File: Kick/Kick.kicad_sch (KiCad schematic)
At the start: 11 parts, among them J1 CN1 / J11, J2 CN2 / J12, U0 NOIP1SN1300A-QTI, U1 NOIP1SN1300A-QTI, U2 NX3L4053, U3 NX3L4053, U4 MIC5504-1.8YM5

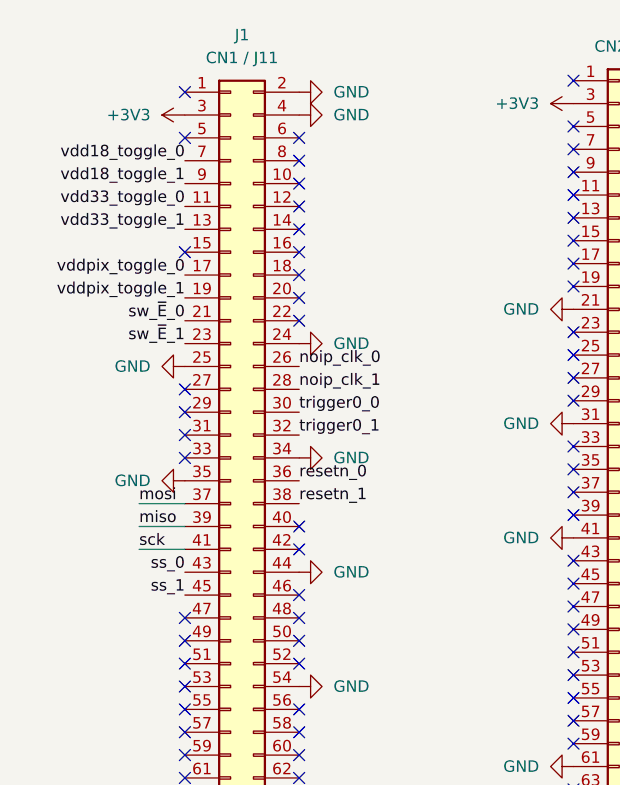
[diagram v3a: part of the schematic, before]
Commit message: routed U1's side and power supply.
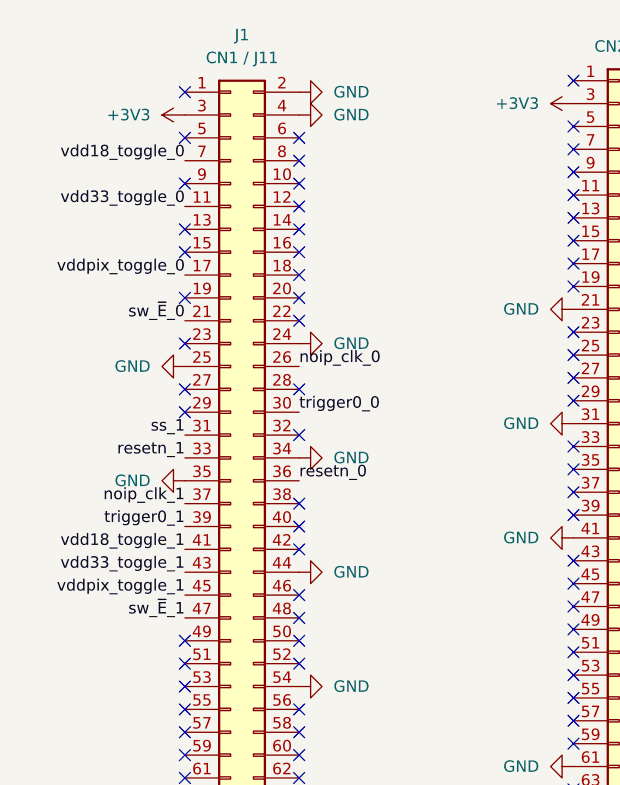
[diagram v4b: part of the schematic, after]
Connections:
- net miso: no longer J1.39 (Pin_39)
- net mosi: no longer J1.37 (Pin_37)
- net noip_clk_1: now also J1.37 (Pin_37); no longer J1.28 (Pin_28)
- net resetn_1: now also J1.33 (Pin_33); no longer J1.38 (Pin_38)
- net sck: no longer J1.41 (Pin_41)
- net ss_0: no longer J1.43 (Pin_43)
- net ss_1: now also J1.31 (Pin_31); no longer J1.45 (Pin_45)
- net sw_~{E}_1: now also J1.47 (Pin_47); no longer J1.23 (Pin_23)
- net trigger0_1: now also J1.39 (Pin_39); no longer J1.32 (Pin_32)
- net vdd18_toggle_1: now also J1.41 (Pin_41); no longer J1.9 (Pin_9)
- net vdd33_toggle_1: now also J1.43 (Pin_43); no longer J1.13 (Pin_13)
- net vddpix_toggle_1: now also J1.45 (Pin_45); no longer J1.19 (Pin_19)
- no-connect marks 102 -> 106

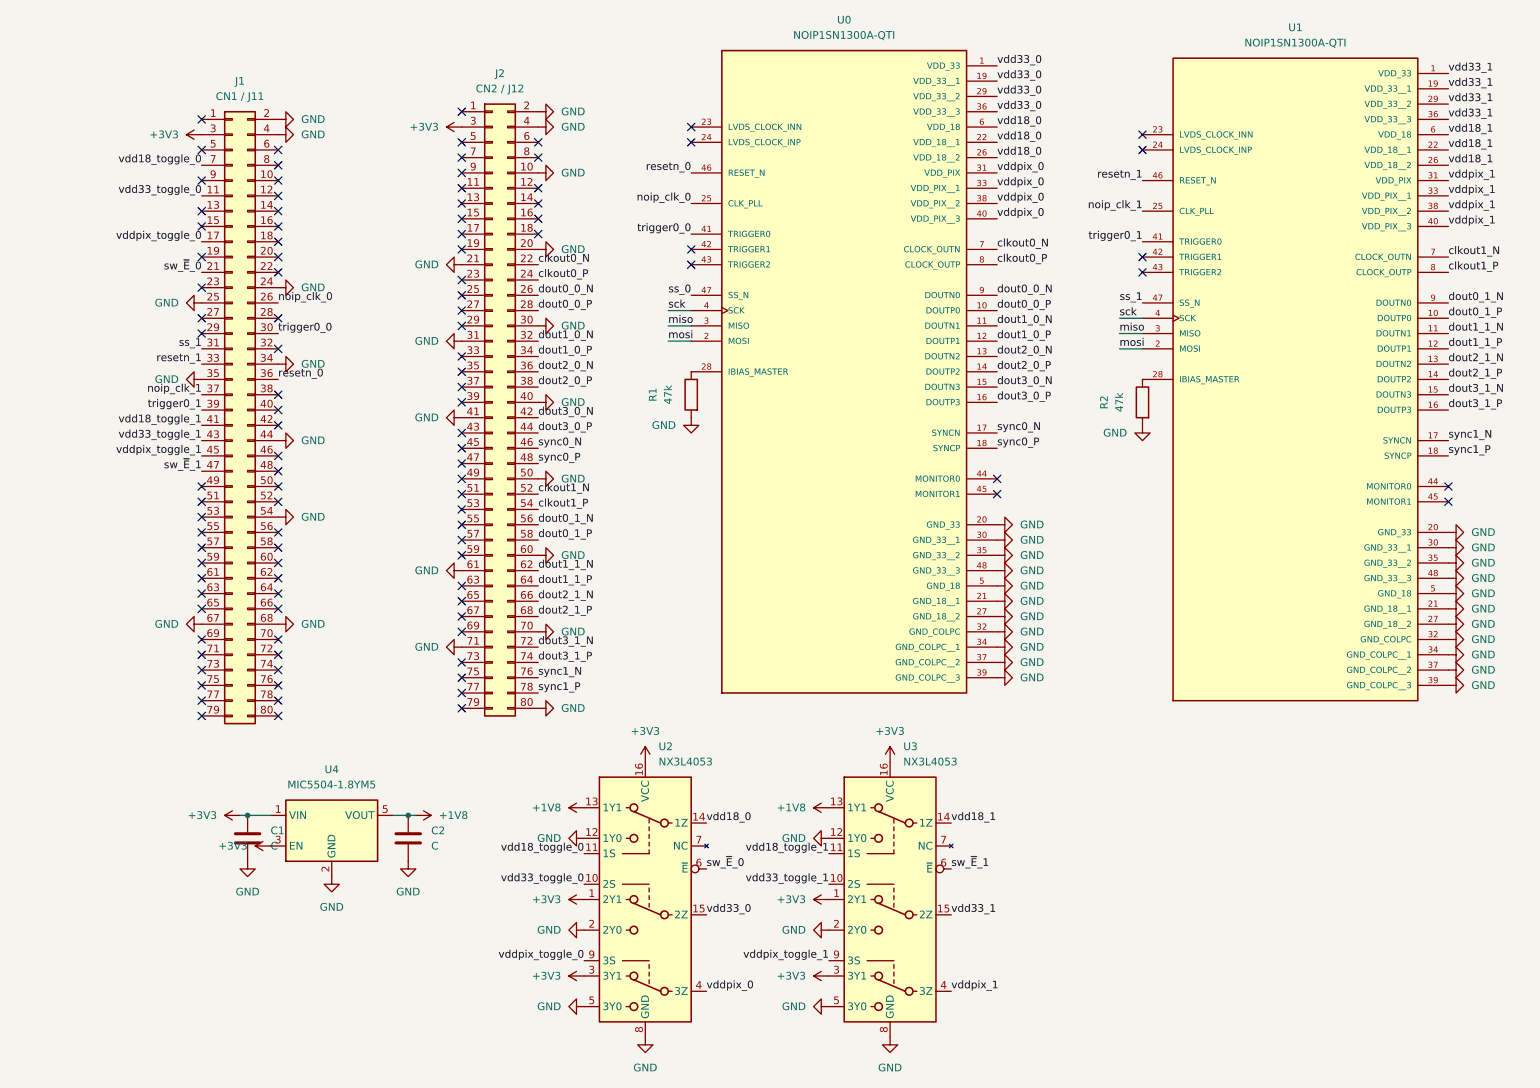
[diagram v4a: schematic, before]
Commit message: preliminary routing (lacking spi and monitors), prior to setting correct distance between sensors
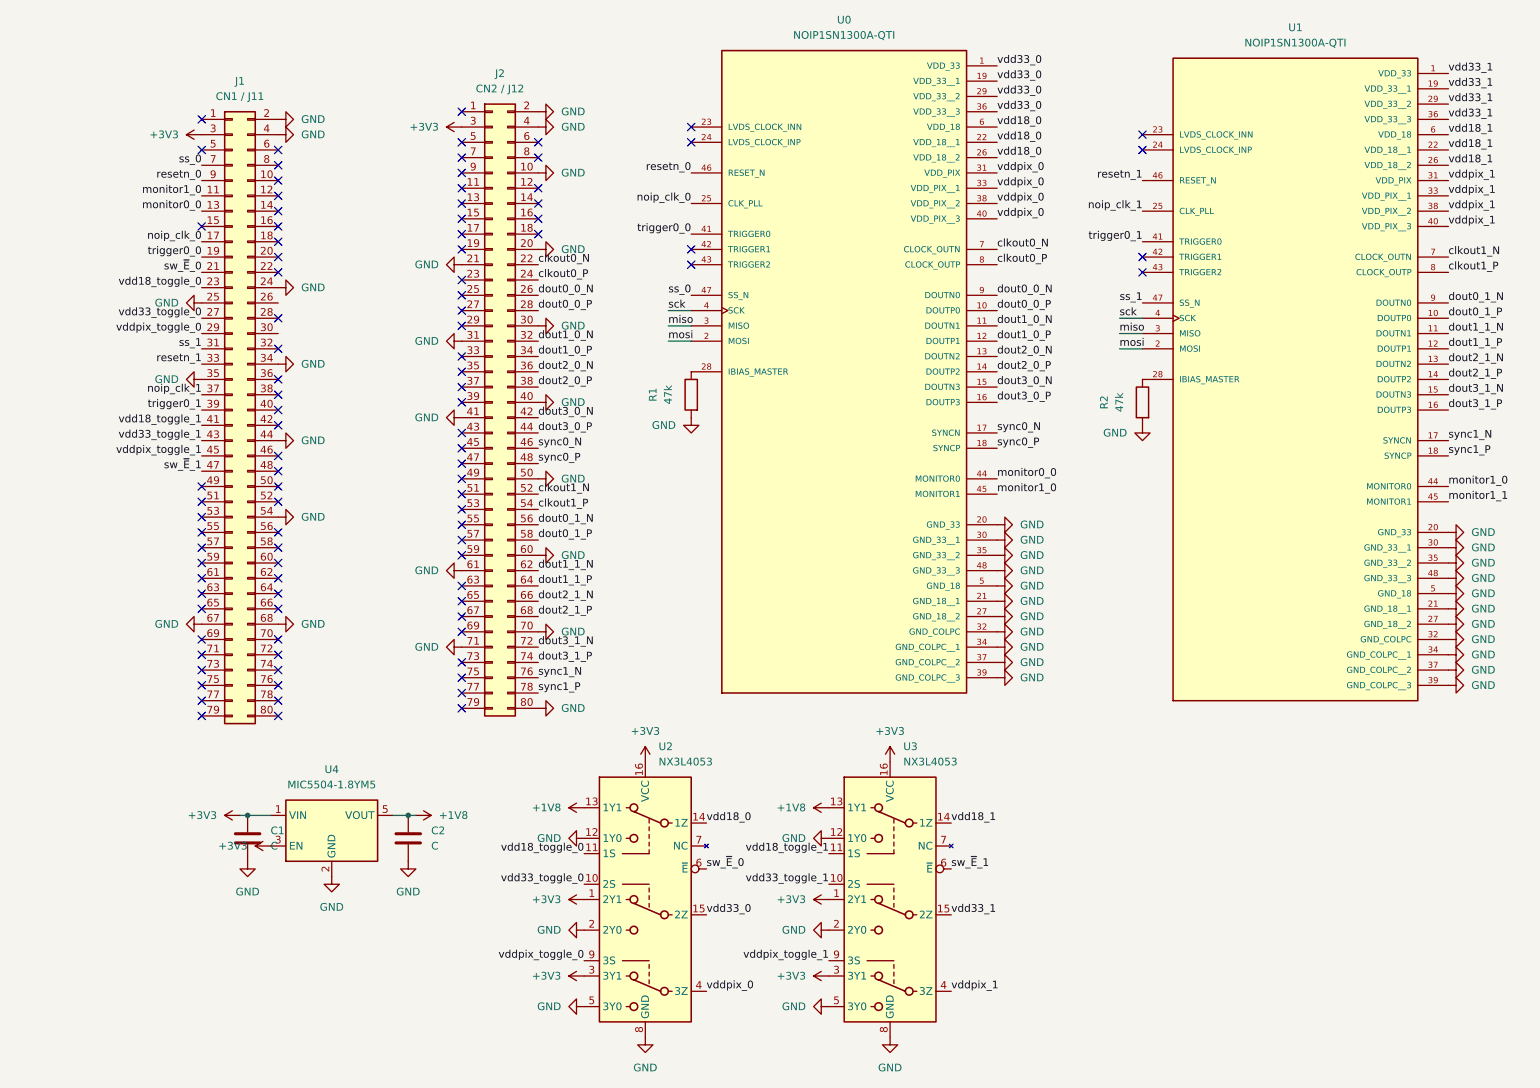
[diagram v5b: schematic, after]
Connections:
- net noip_clk_0: now also J1.17 (Pin_17); no longer J1.26 (Pin_26)
- net resetn_0: now also J1.9 (Pin_9); no longer J1.36 (Pin_36)
- net ss_0: now also J1.7 (Pin_7)
- net trigger0_0: now also J1.19 (Pin_19); no longer J1.30 (Pin_30)
- net vdd18_toggle_0: now also J1.23 (Pin_23); no longer J1.7 (Pin_7)
- net vdd33_toggle_0: now also J1.27 (Pin_27); no longer J1.11 (Pin_11)
- net vddpix_toggle_0: now also J1.29 (Pin_29); no longer J1.17 (Pin_17)
- net monitor0_0: now reaches J1.13 (Pin_13)
- net monitor0_0: now also U0.44 (MONITOR0)
- net monitor1_0: now reaches U0.45 (MONITOR1)
- net monitor1_0: now also J1.11 (Pin_11), U1.44 (MONITOR0)
- net monitor1_1: now reaches U1.45 (MONITOR1)
- no-connect marks 106 -> 97

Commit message: finished routing and drc
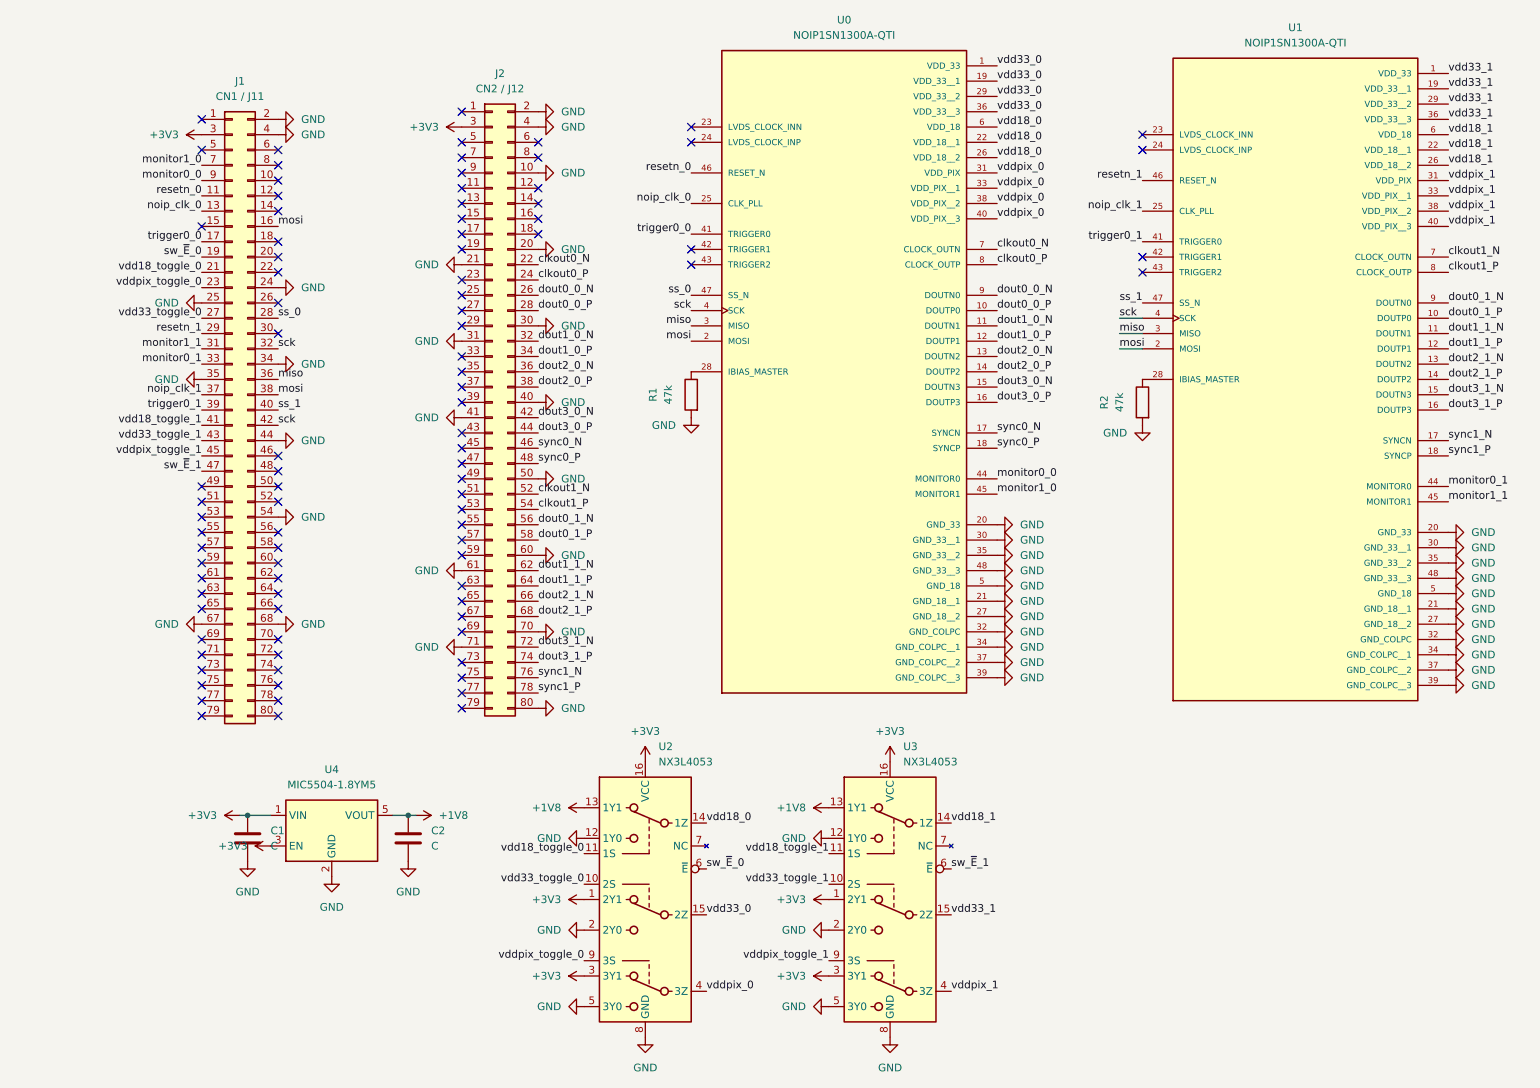
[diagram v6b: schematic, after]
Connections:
- net miso: now also J1.36 (Pin_36)
- net monitor0_0: now also J1.9 (Pin_9); no longer J1.13 (Pin_13)
- net monitor1_0: now also J1.7 (Pin_7); no longer J1.11 (Pin_11), U1.44 (MONITOR0)
- net monitor1_1: now also J1.31 (Pin_31)
- net mosi: now also J1.16 (Pin_16), J1.38 (Pin_38)
- net noip_clk_0: now also J1.13 (Pin_13); no longer J1.17 (Pin_17)
- net resetn_0: now also J1.11 (Pin_11); no longer J1.9 (Pin_9)
- net resetn_1: now also J1.29 (Pin_29); no longer J1.33 (Pin_33)
- net sck: now also J1.32 (Pin_32), J1.42 (Pin_42)
- net ss_0: now also J1.28 (Pin_28); no longer J1.7 (Pin_7)
- net ss_1: now also J1.40 (Pin_40); no longer J1.31 (Pin_31)
- net sw_~{E}_0: now also J1.19 (Pin_19); no longer J1.21 (Pin_21)
- net trigger0_0: now also J1.17 (Pin_17); no longer J1.19 (Pin_19)
- net vdd18_toggle_0: now also J1.21 (Pin_21); no longer J1.23 (Pin_23)
- net vddpix_toggle_0: now also J1.23 (Pin_23); no longer J1.29 (Pin_29)
- new net monitor0_1: J1.33 (Pin_33), U1.44 (MONITOR0)
- no-connect marks 97 -> 92

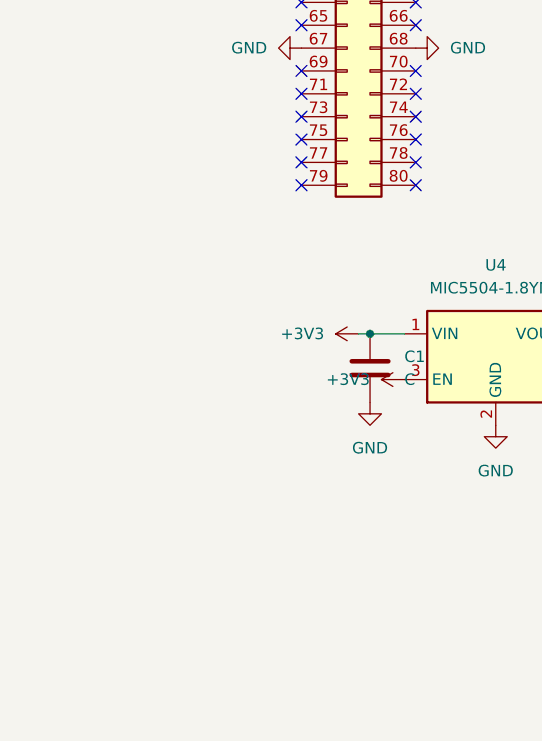
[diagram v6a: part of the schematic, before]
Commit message: decoupled noip power pins
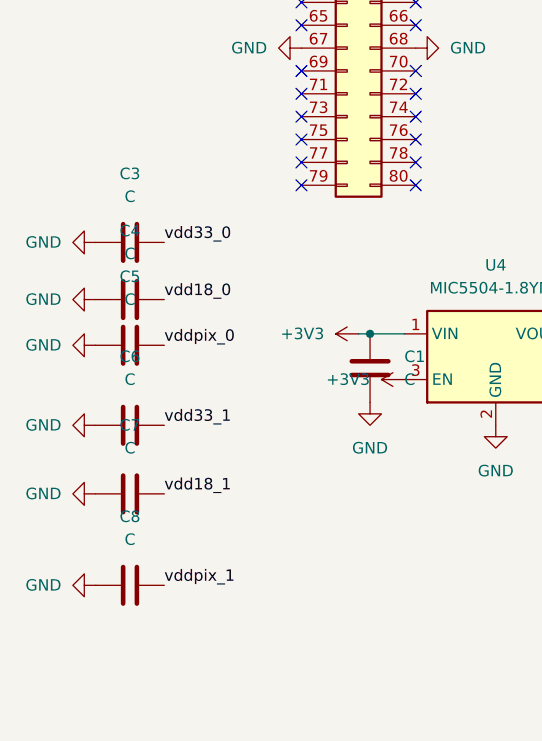
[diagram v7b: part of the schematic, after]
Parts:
- added C3, C4, C5, C6, C7, C8: C, Capacitor_SMD:C_0603_1608Metric, symbol Device:C
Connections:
- net GND: now also C3.1, C4.1, C5.1, C6.1, C7.1, C8.1
- net vdd18_0: now also C4.2
- net vdd18_1: now also C7.2
- net vdd33_0: now also C3.2
- net vdd33_1: now also C6.2
- net vddpix_0: now also C5.2
- net vddpix_1: now also C8.2

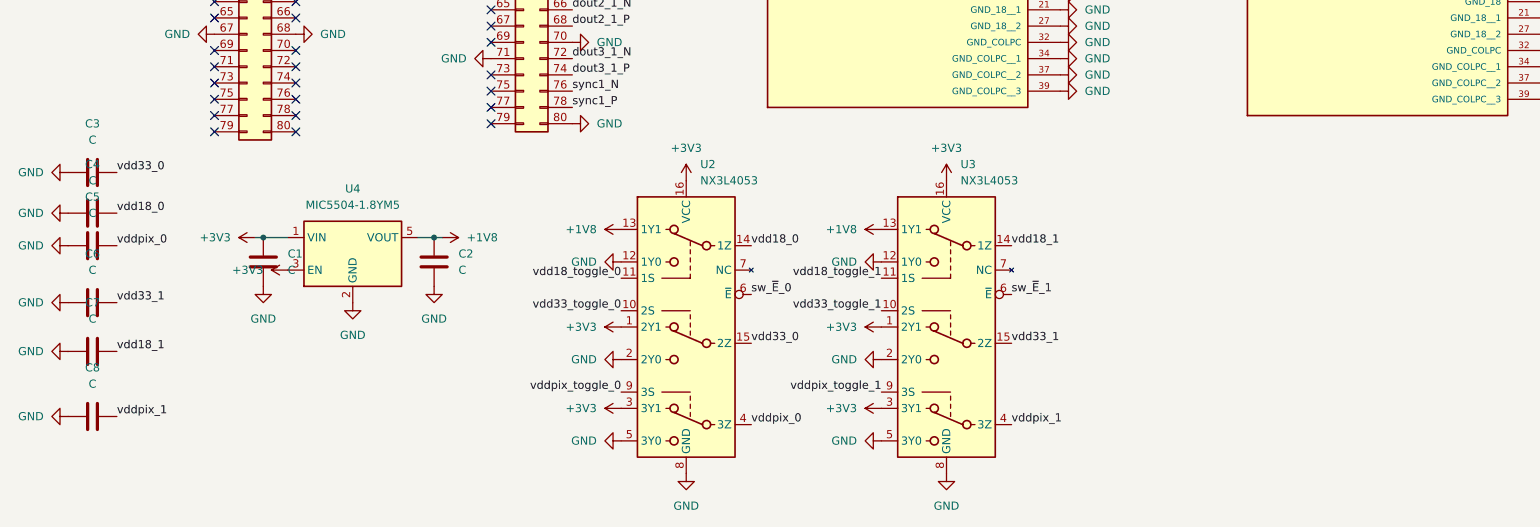
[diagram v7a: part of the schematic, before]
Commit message: issue #4 : decoupled ALL power pairs of sensors and added decoupling caps to schematic for easy reference
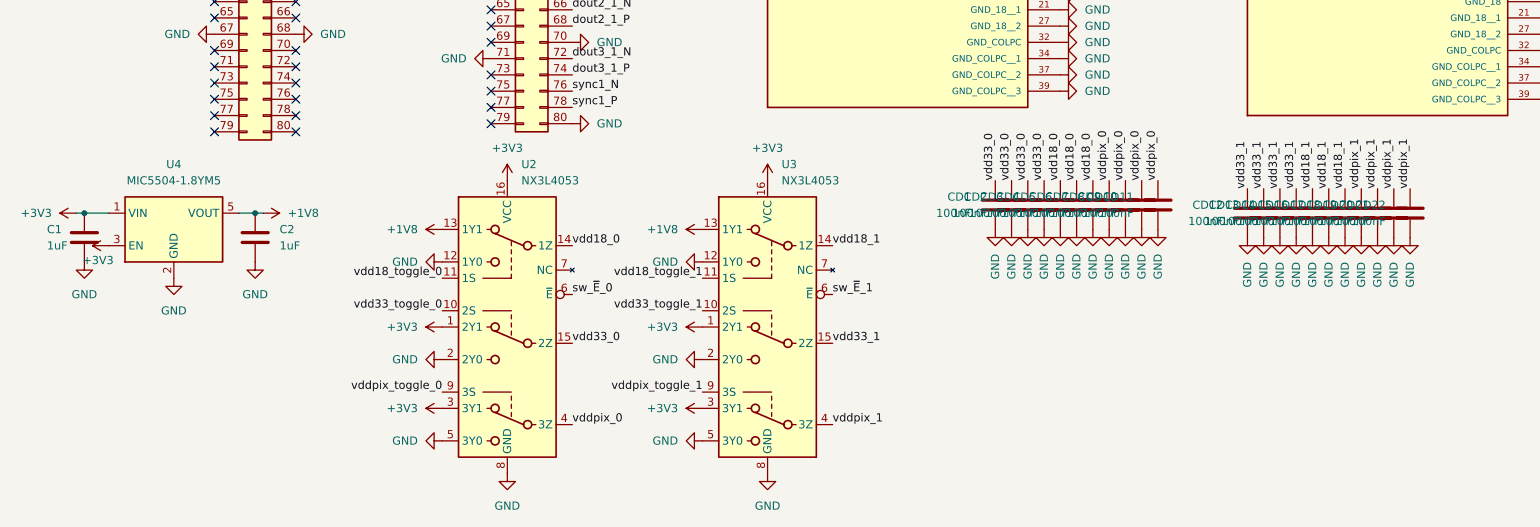
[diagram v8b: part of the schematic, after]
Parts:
- removed C3, C4, C5, C6, C7, C8: C, Capacitor_SMD:C_0603_1608Metric, symbol Device:C
- added CD1, CD10, CD11, CD12, CD13, CD14, CD15, CD16, CD17, CD18, CD19, CD2, CD20, CD21, CD22, CD3, CD4, CD5, CD6, CD7, CD8, CD9: 100nF, Capacitor_SMD:C_0603_1608Metric, symbol Device:C
- C1, C2: value C -> 1uF
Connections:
- net GND: now also CD1.2, CD10.2, CD11.2, CD12.2, CD13.2, CD14.2, CD15.2, CD16.2, CD17.2, CD18.2, CD19.2, CD2.2, CD20.2, CD21.2, CD22.2, CD3.2, CD4.2, CD5.2, CD6.2, CD7.2, CD8.2, CD9.2
- net vdd18_0: now also CD5.1, CD6.1, CD7.1
- net vdd18_1: now also CD16.1, CD17.1, CD18.1
- net vdd33_0: now also CD1.1, CD2.1, CD3.1, CD4.1
- net vdd33_1: now also CD12.1, CD13.1, CD14.1, CD15.1
- net vddpix_0: now also CD10.1, CD11.1, CD8.1, CD9.1
- net vddpix_1: now also CD19.1, CD20.1, CD21.1, CD22.1
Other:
- moved on the sheet: C1, C2, U2, U3, U4
